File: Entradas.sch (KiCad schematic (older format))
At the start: 1 part

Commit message: Se completaron los circuitos esquematicos, falta revision.
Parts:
- added D5, D6: LED, symbol LED
- added Enc_r1: Encoder_rotativo, symbol Encoder_rotativo
- added J3: TB_1X3, symbol TB_1X3
- added R10, R16, R5, R8, R9: 4K7, symbol R
- added R11, R13: 2K2, symbol R
- added R12, R14: 100K, symbol R
- added R15: 220, symbol R
- added R6, R7: 3K3, symbol R
- added U1, U2: PS2805-1, SSOP-4, symbol PS2805-1
- added U3: CNY70, symbol CNY70
- gave numbers to parts that had none: 1
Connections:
- net GND: now also Enc_r1.2 (C), R15.2, R16.2, U1.3, U2.3
- new net: R10.1, R7.1, U2.1
- new net: R13.1, R14.1
- new net: D6.2 (A), R13.2
- new net: R6.1, R8.1, U1.1
- new net: R11.1, R12.1
- new net: D5.2 (A), R11.2
- new net: R15.1, U3.2 (CAT)
- new net +3V3: R5.1, R9.1, U3.1 (AN), U3.4 (COL)
- new net CNY_IN: R16.1, U3.3 (EM)
- new net COM: J3.2, R10.2, R8.2, U1.2, U2.2
- new net Encoder_A: Enc_r1.1 (A), R9.2
- new net Encoder_B: Enc_r1.3 (B), R5.2
- new net IN0: J3.1, R7.2
- new net IN1: J3.3, R6.2
- new net OPTO_IN0: D6.1 (K), R14.2, U2.4
- new net OPTO_IN1: D5.1 (K), R12.2, U1.4
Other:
- note added: "CNY-70"
- note added: "Encoder Rotativo"
- note added: "Entradas Optoacopladas"
- note added: "Potenciometro"
- moved on the sheet: R17

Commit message: se agregaron casi todos los footprint faltan el conector del poncho, encoder y CNY70
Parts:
- D5, D6: footprint (none) -> LEDs:LED_0603
- J3: footprint (none) -> Terminal_Blocks:TerminalBlock_Pheonix_PT-3.5mm_3pol
- R10, R11, R12, R13, R14, R15, R16, R5, R6, R7, R8, R9: footprint (none) -> Resistors_SMD:R_0603_HandSoldering
- R17: footprint (none) -> Potentiometers:Potentiometer_Alps-RK16-single_largePads
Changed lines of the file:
@@
 EESchema Schematic File Version 2
 LIBS:device
-LIBS:dsp
 LIBS:power
 LIBS:sensors
@@
 LIBS:switches
 LIBS:references
-LIBS:maxim
-LIBS:atmel
-LIBS:motorola
 LIBS:interface
 LIBS:cmos_ieee
 LIBS:analog_devices
 LIBS:nordicsemi
-LIBS:microchip_pic32mcu
 LIBS:74xgxx
 LIBS:transistors
-LIBS:philips
 LIBS:nxp_armmcu
-LIBS:supertex
 LIBS:logo
 LIBS:Power_Management
@@
 LIBS:contrib
 LIBS:cmos4000
-LIBS:ac-dc
-LIBS:memory
-LIBS:digital-audio
-LIBS:rfcom
-LIBS:video
-LIBS:microchip_pic16mcu
-LIBS:microchip_pic10mcu
-LIBS:onsemi
-LIBS:brooktre
-LIBS:Oscillators
-LIBS:stm32
 LIBS:elec-unifil
 LIBS:graphic
 LIBS:display
-LIBS:intel
-LIBS:Zilog
 LIBS:dc-dc
-LIBS:ftdi
-LIBS:microchip_pic18mcu
-LIBS:msp430
-LIBS:hc11
-LIBS:Lattice
-LIBS:cypress
-LIBS:Xicor
-LIBS:silabs
-LIBS:microchip
 LIBS:opto
 LIBS:transf
@@
 LIBS:pspice
 LIBS:xilinx
-LIBS:Symbols_EN60617_13Mar2013
-LIBS:Symbols_EN60617-10_HF-Radio_DRAFT_12Sep2013
-LIBS:Symbols_Transformer-Diskrete_RevA
-LIBS:Symbols_ICs-Diskrete_RevD10
-LIBS:Symbols_ICs-Opto_RevB_16Sep2013
-LIBS:Symbols_Socket-DIN41612_RevA
-LIBS:Symbols_DCDC-ACDC-Converter_RevC_20Jul2012
-LIBS:Symbols_Microcontroller_Philips-NXP_RevA_06Oct2013
-LIBS:SymbolsSimilarEN60617+oldDIN617-RevE8
 LIBS:w_device
 LIBS:tvs
@@
 LIBS:pbss5240xf
 LIBS:nsi50010yt1g
-LIBS:net-phy
 LIBS:mcu-st
-LIBS:mcu-nxp
-LIBS:mcp1416
-LIBS:mcp1415
-LIBS:lm2596
-LIBS:g5v2
 LIBS:fqt13n06l
 LIBS:bat54_c
-LIBS:audio-vlsi
-LIBS:amesser-usb
 LIBS:amesser-power
 LIBS:amesser-linear
@@
 LIBS:amesser-ad
 LIBS:Transil_diode
-LIBS:TXB0108
-LIBS:TJA1040
-LIBS:Si50x
-LIBS:SCHA5B0200
 LIBS:PS2805
-LIBS:PRTR5V0U2X
-LIBS:PBSS5240
-LIBS:MIC2025
-LIBS:LPC4337JBD144
-LIBS:IS42S16400F
-LIBS:FT2232H
 LIBS:BLM15HG6015N1D
 LIBS:93CXX
@@
 F 0 "R17" H 8100 4950 50  0000 C CNN
 F 1 "5K" H 8100 4500 50  0000 C CNN
-F 2 "" H 8100 4650 50  0000 C CNN
+F 2 "Potentiometers:Potentiometer_Alps-RK16-single_largePads" H 8100 4650 50  0001 C CNN
 F 3 "" H 8100 4650 50  0000 C CNN
 	1    8100 4650
@@
 F 0 "R10" V 2930 2150 50  0000 C CNN
 F 1 "4K7" V 2850 2150 50  0000 C CNN
-F 2 "" V 2780 2150 50  0000 C CNN
+F 2 "Resistors_SMD:R_0603_HandSoldering" V 2780 2150 50  0001 C CNN
 F 3 "" H 2850 2150 50  0000 C CNN
 	1    2850 2150
@@
 F 0 "R7" V 2680 1950 50  0000 C CNN
 F 1 "3K3" V 2600 1950 50  0000 C CNN
-F 2 "" V 2530 1950 50  0000 C CNN
+F 2 "Resistors_SMD:R_0603_HandSoldering" V 2530 1950 50  0001 C CNN
 F 3 "" H 2600 1950 50  0000 C CNN
 	1    2600 1950
@@
 F 0 "R13" V 4780 1800 50  0000 C CNN
 F 1 "2K2" V 4700 1800 50  0000 C CNN
-F 2 "" V 4630 1800 50  0000 C CNN
+F 2 "Resistors_SMD:R_0603_HandSoldering" V 4630 1800 50  0001 C CNN
 F 3 "" H 4700 1800 50  0000 C CNN
 	1    4700 1800
@@
 F 0 "R14" V 4780 2050 50  0000 C CNN
 F 1 "100K" V 4700 2050 50  0000 C CNN
-F 2 "" V 4630 2050 50  0000 C CNN
+F 2 "Resistors_SMD:R_0603_HandSoldering" V 4630 2050 50  0001 C CNN
 F 3 "" H 4700 2050 50  0000 C CNN
 	1    4700 2050
@@
 F 0 "D6" H 4200 1900 50  0000 C CNN
 F 1 "LED" H 4200 1700 50  0000 C CNN
-F 2 "" H 4200 1800 50  0000 C CNN
+F 2 "LEDs:LED_0603" H 4200 1800 50  0001 C CNN
 F 3 "" H 4200 1800 50  0000 C CNN
 	1    4200 1800
@@
 F 0 "Enc_r1" H 3850 5400 50  0000 C CNN
 F 1 "Encoder_rotativo" H 3750 4701 50  0000 C CNN
-F 2 "" H 3750 5050 50  0000 C CNN
+F 2 "" H 3750 5050 50  0001 C CNN
 F 3 "" H 3750 5050 50  0000 C CNN
 	1    3750 5050
@@
 F 0 "R9" V 2880 4550 50  0000 C CNN
 F 1 "4K7" V 2800 4550 50  0000 C CNN
-F 2 "" V 2730 4550 50  0000 C CNN
+F 2 "Resistors_SMD:R_0603_HandSoldering" V 2730 4550 50  0001 C CNN
 F 3 "" H 2800 4550 50  0000 C CNN
 	1    2800 4550
@@
 F 0 "R5" V 2580 4550 50  0000 C CNN
 F 1 "4K7" V 2500 4550 50  0000 C CNN
-F 2 "" V 2430 4550 50  0000 C CNN
+F 2 "Resistors_SMD:R_0603_HandSoldering" V 2430 4550 50  0001 C CNN
 F 3 "" H 2500 4550 50  0000 C CNN
 	1    2500 4550
@@
 F 0 "J3" H 1400 2850 60  0000 C CNN
 F 1 "TB_1X3" H 1450 2100 60  0000 C CNN
-F 2 "" H 1350 2600 60  0000 C CNN
+F 2 "Terminal_Blocks:TerminalBlock_Pheonix_PT-3.5mm_3pol" H 1350 2600 60  0001 C CNN
 F 3 "" H 1350 2600 60  0000 C CNN
 	1    1400 2550
@@
 F 0 "R8" V 2880 3150 50  0000 C CNN
 F 1 "4K7" V 2800 3150 50  0000 C CNN
-F 2 "" V 2730 3150 50  0000 C CNN
+F 2 "Resistors_SMD:R_0603_HandSoldering" V 2730 3150 50  0001 C CNN
 F 3 "" H 2800 3150 50  0000 C CNN
 	1    2800 3150
@@
 F 0 "R6" V 2630 2950 50  0000 C CNN
 F 1 "3K3" V 2550 2950 50  0000 C CNN
-F 2 "" V 2480 2950 50  0000 C CNN
+F 2 "Resistors_SMD:R_0603_HandSoldering" V 2480 2950 50  0001 C CNN
 F 3 "" H 2550 2950 50  0000 C CNN
 	1    2550 2950
@@
 F 0 "R11" V 4730 2800 50  0000 C CNN
 F 1 "2K2" V 4650 2800 50  0000 C CNN
-F 2 "" V 4580 2800 50  0000 C CNN
+F 2 "Resistors_SMD:R_0603_HandSoldering" V 4580 2800 50  0001 C CNN
 F 3 "" H 4650 2800 50  0000 C CNN
 	1    4650 2800
@@
 F 0 "R12" V 4730 3050 50  0000 C CNN
 F 1 "100K" V 4650 3050 50  0000 C CNN
-F 2 "" V 4580 3050 50  0000 C CNN
+F 2 "Resistors_SMD:R_0603_HandSoldering" V 4580 3050 50  0001 C CNN
 F 3 "" H 4650 3050 50  0000 C CNN
 	1    4650 3050
@@
 F 0 "D5" H 4150 2900 50  0000 C CNN
 F 1 "LED" H 4150 2700 50  0000 C CNN
-F 2 "" H 4150 2800 50  0000 C CNN
+F 2 "LEDs:LED_0603" H 4150 2800 50  0001 C CNN
 F 3 "" H 4150 2800 50  0000 C CNN
 	1    4150 2800
@@
 F 0 "U3" H 7390 2340 50  0000 L CNN
 F 1 "CNY70" H 7600 2350 50  0000 L CNN
-F 2 "" H 7400 1950 50  0000 L CIN
+F 2 "" H 7400 1950 50  0001 L CIN
 F 3 "" H 7600 2150 50  0000 L CNN
 	1    7600 2150
@@
 F 0 "R15" V 7330 2550 50  0000 C CNN
 F 1 "220" V 7250 2550 50  0000 C CNN
-F 2 "" V 7180 2550 50  0000 C CNN
+F 2 "Resistors_SMD:R_0603_HandSoldering" V 7180 2550 50  0001 C CNN
 F 3 "" H 7250 2550 50  0000 C CNN
 	1    7250 2550
@@
 F 0 "R16" V 8030 2550 50  0000 C CNN
 F 1 "4K7" V 7950 2550 50  0000 C CNN
-F 2 "" V 7880 2550 50  0000 C CNN
+F 2 "Resistors_SMD:R_0603_HandSoldering" V 7880 2550 50  0001 C CNN
 F 3 "" H 7950 2550 50  0000 C CNN
 	1    7950 2550

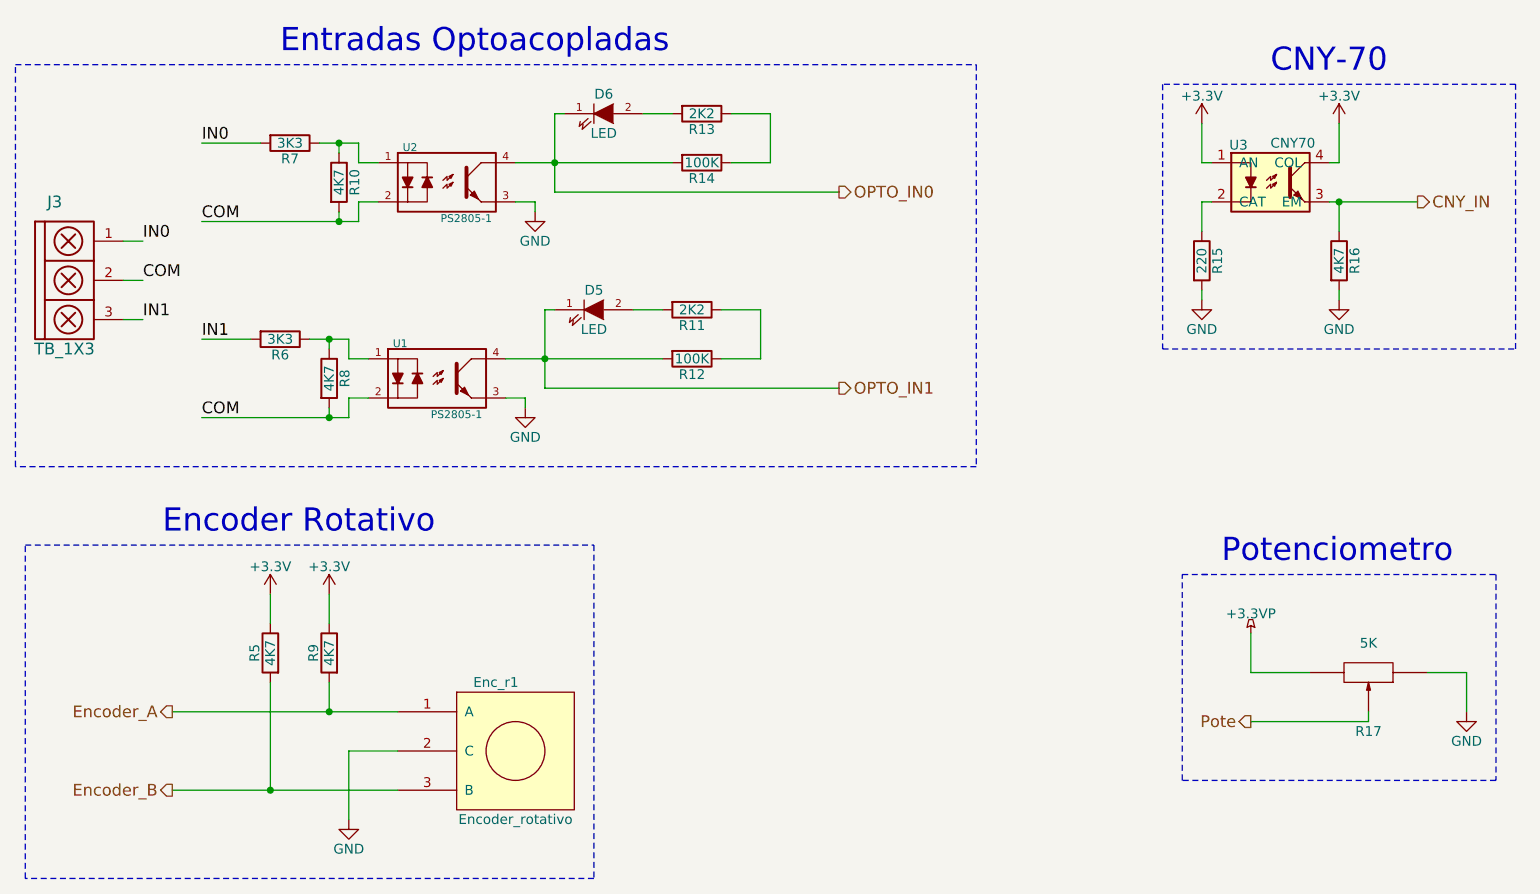
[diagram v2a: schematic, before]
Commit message: Correcion de errores, asignacion de footprints y ubicacion prelimilar de componentes.
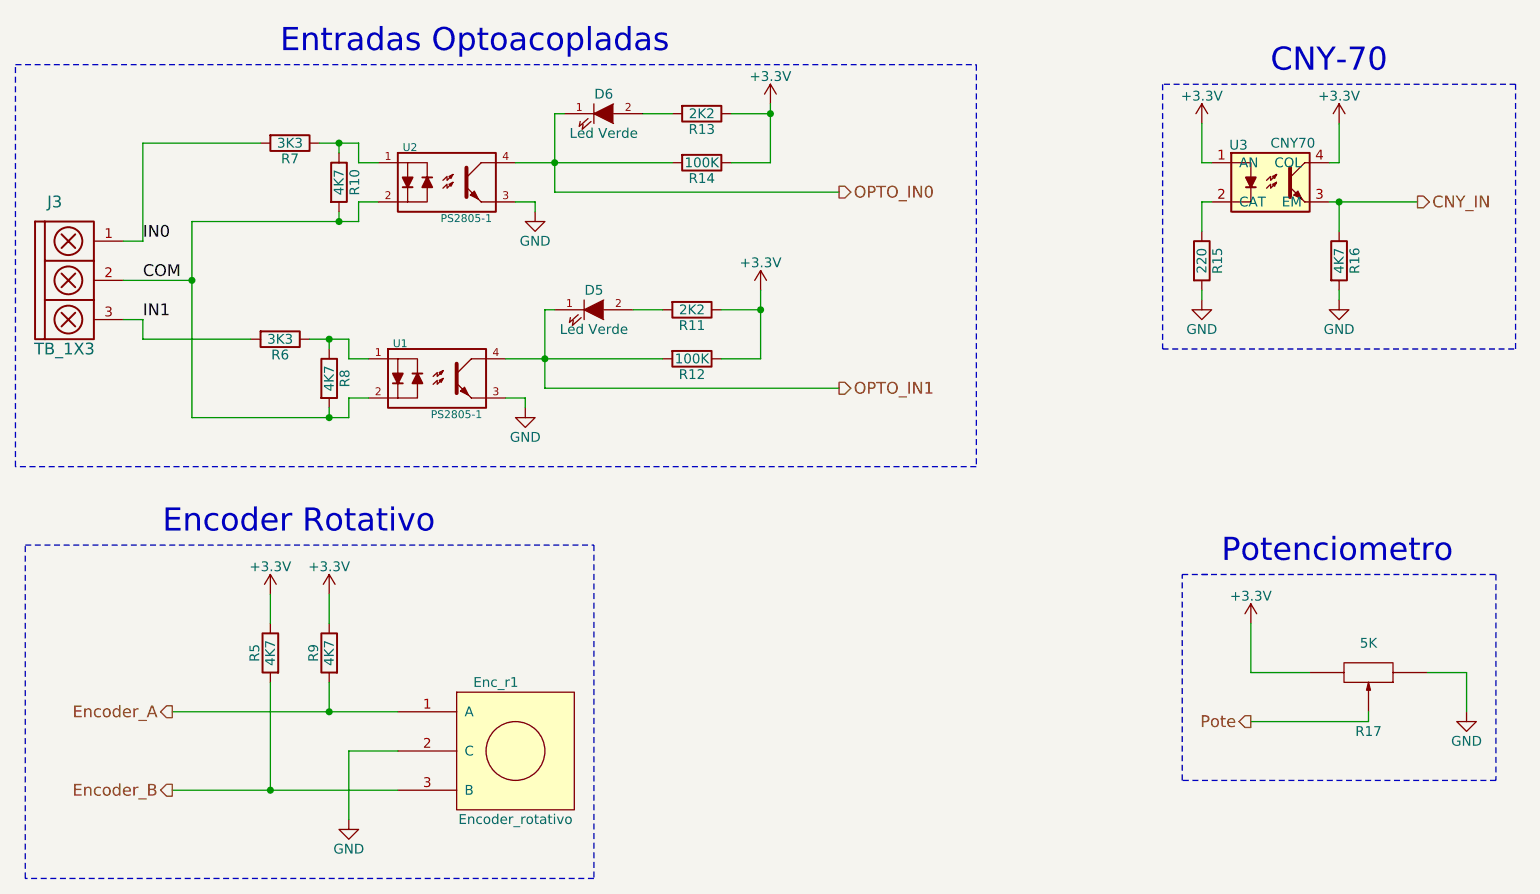
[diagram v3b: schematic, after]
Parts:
- D5, D6: value LED -> Led Verde
- Enc_r1: footprint (none) -> Potentiometers:Potentiometer_Alps-RK16-single_largePads; Digikey# (none) -> 987-1190-ND
- R10, R11, R12, R13, R14, R15, R16, R5, R6, R7, R8, R9: footprint Resistors_SMD:R_0603_HandSoldering -> Resistors_SMD:R_1206_HandSoldering
- U1, U2: footprint SSOP-4 -> Opto-Devices:Optocoupler_SMD_HandSoldering_KPC357_LTV35x_PC357_SingleChannel
- U3: footprint (none) -> footprint:CNY70
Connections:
- net +3.3VP is gone; now on net +3V3: R17.3
- net +3V3: now also R11.1, R12.1, R13.1, R14.1

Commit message: Se termino de rutear la placa y se acomodaron ref de los componentes, se agrego nombres y fiduciales
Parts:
- Enc_r1: Digikey# 987-1190-ND -> 987-1193-ND
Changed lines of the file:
@@
 F 2 "Potentiometers:Potentiometer_Alps-RK16-single_largePads" H 3750 5050 50  0001 C CNN
 F 3 "" H 3750 5050 50  0000 C CNN
-F 4 "987-1190-ND" H 3750 5050 60  0001 C CNN "Digikey#"
+F 4 "987-1193-ND" H 3750 5050 60  0001 C CNN "Digikey#"
 	1    3750 5050
 	-1   0    0    -1

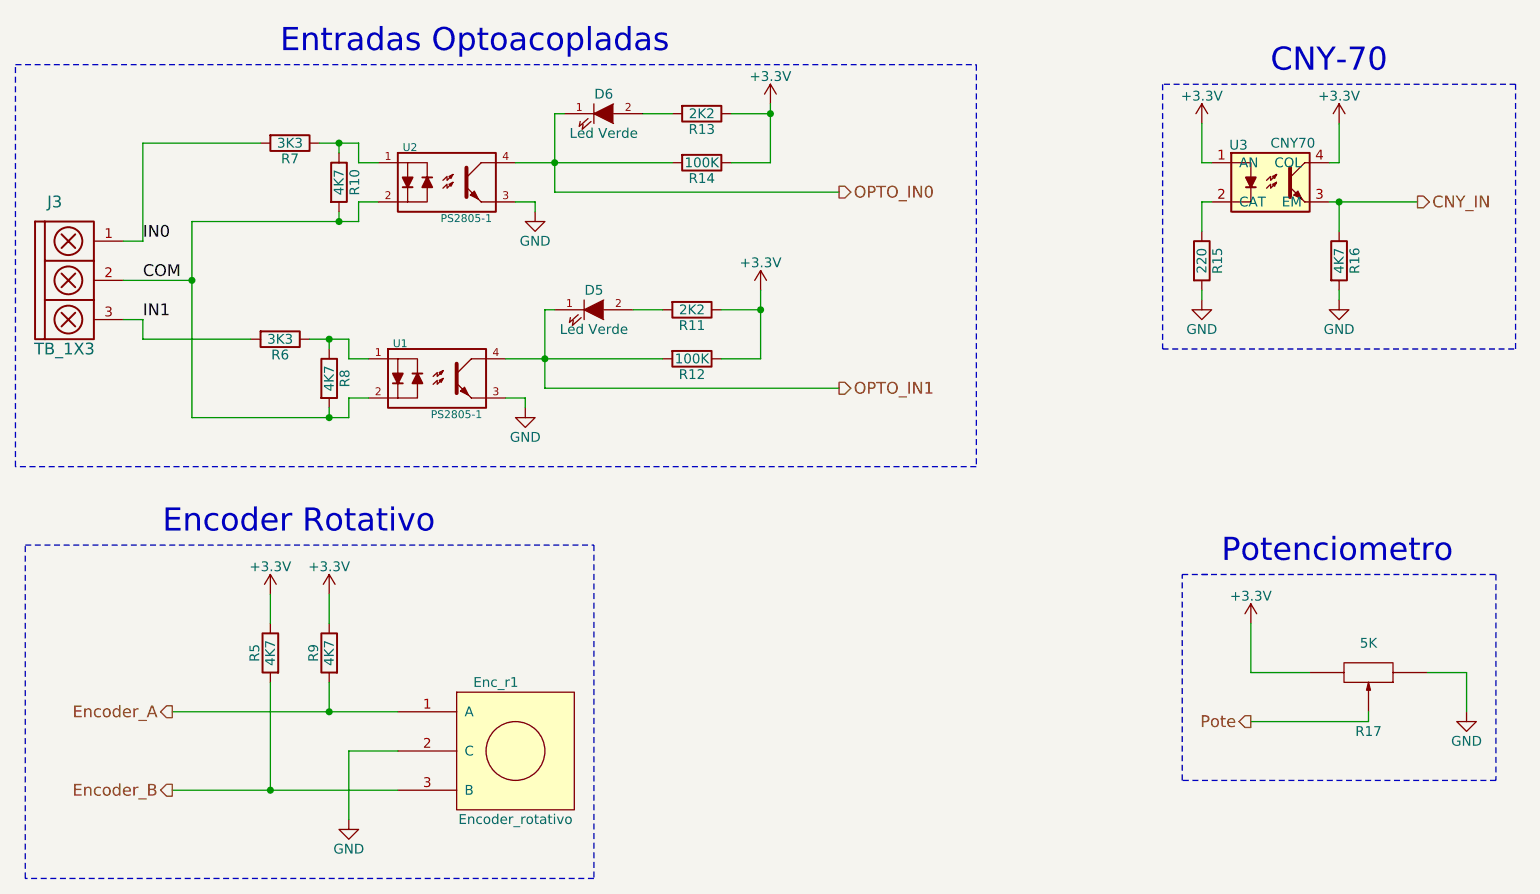
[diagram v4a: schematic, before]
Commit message: Reubicacion de optoacopladores, cambio de footoprins de resistencias a 0805, correcion general.Falta arreglar archivos vista 3d y completar los campos #digikey
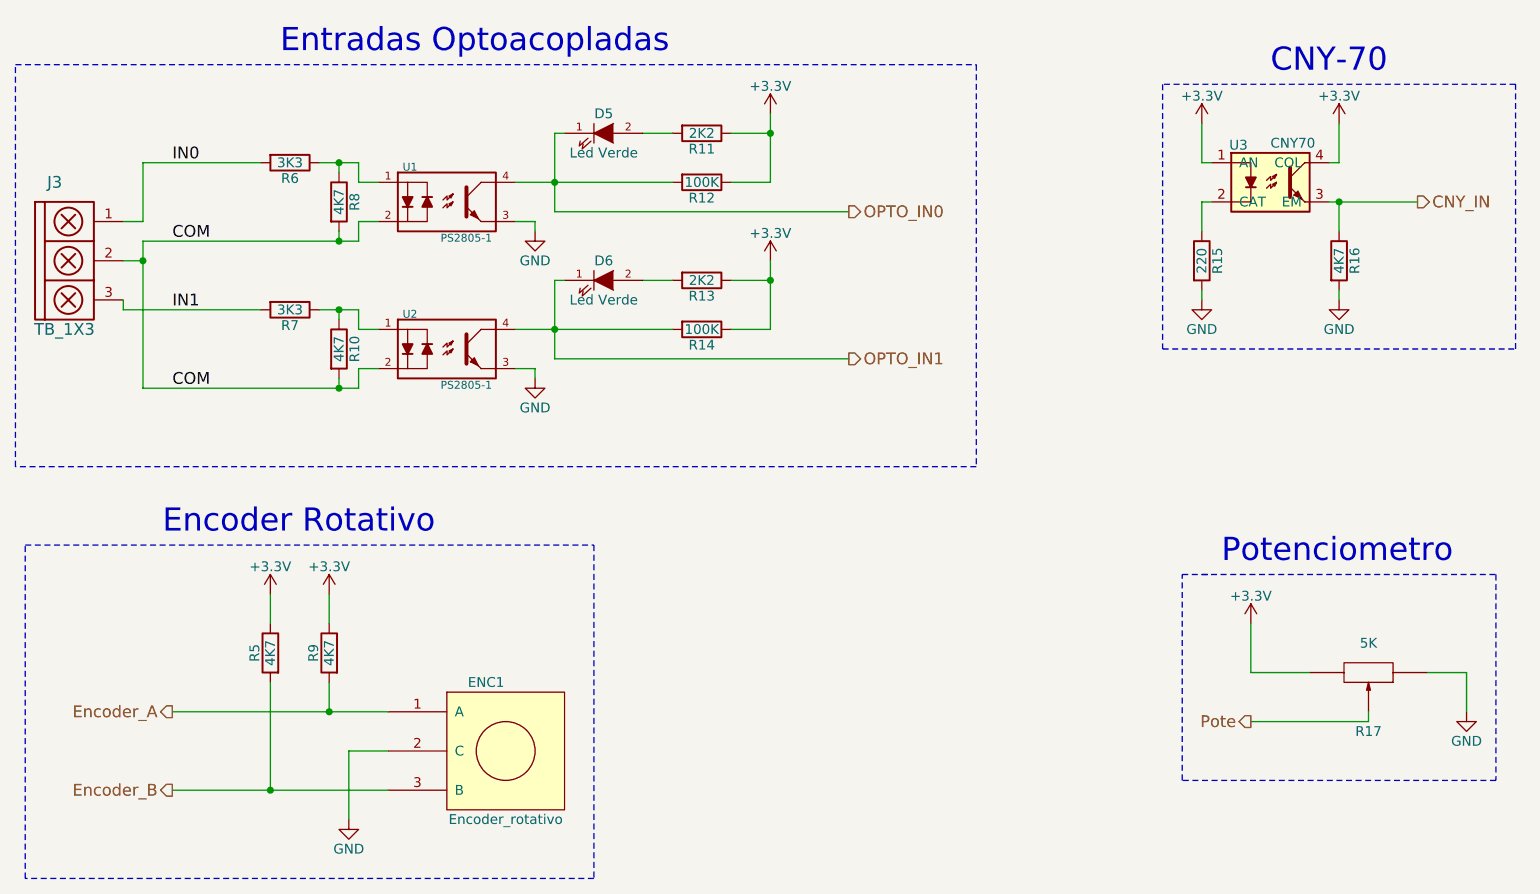
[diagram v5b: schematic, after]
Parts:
- removed Enc_r1: Encoder_rotativo, Potentiometers:Potentiometer_Alps-RK16-single_largePads, symbol Encoder_rotativo
- added ENC1: Encoder_rotativo, footprint:Encoder_rotativo, symbol Encoder_rotativo
- J3: footprint Terminal_Blocks:TerminalBlock_Pheonix_PT-3.5mm_3pol -> Terminal_Blocks:TerminalBlock_Pheonix_MPT-2.54mm_3pol
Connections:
- net Encoder_A: now also ENC1.1 (A)
- net Encoder_B: now also ENC1.3 (B)
- net GND: now also ENC1.2 (C)
- net IN0: now also R6.2; no longer R7.2
- net IN1: now also R7.2; no longer R6.2
- net OPTO_IN0: now also D5.1 (K), R12.2, U1.4; no longer D6.1 (K), R14.2, U2.4
- net OPTO_IN1: now also D6.1 (K), R14.2, U2.4; no longer D5.1 (K), R12.2, U1.4
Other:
- moved on the sheet: D5, R11, R12, R6, R8, U1
